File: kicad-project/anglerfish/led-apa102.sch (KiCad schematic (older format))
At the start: 2 parts

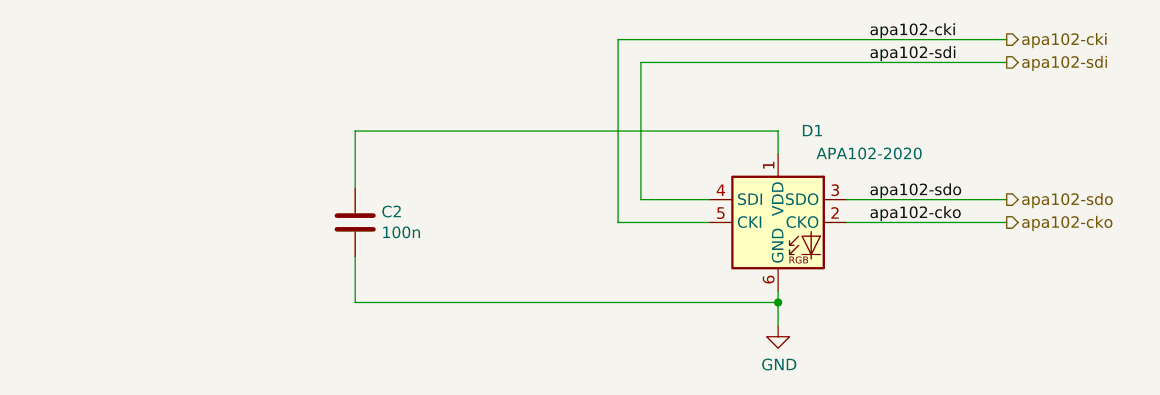
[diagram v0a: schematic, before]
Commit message: Generated gerbers. I discovered that I was working in a temp folder, so I erased the files under the anglerfish folder and manually brought the files from the temp folder.
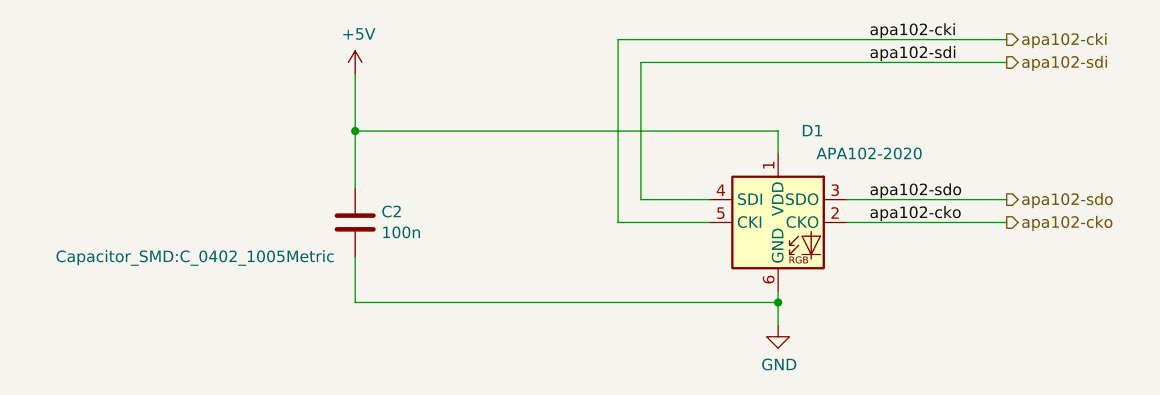
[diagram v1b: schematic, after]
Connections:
- net +5V: now reaches C2.1, D1.1 (VDD)
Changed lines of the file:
@@
 F 0 "C2" H 3615 3596 50  0000 L CNN
 F 1 "100n" H 3615 3505 50  0000 L CNN
-F 2 "Capacitor_SMD:C_0402_1005Metric" H 3538 3400 50  0001 C CNN
+F 2 "Capacitor_SMD:C_0402_1005Metric" H 2800 3400 50  0000 C CNN
 F 3 "~" H 3500 3550 50  0001 C CNN
 	1    3500 3550
@@
 Text Label 5750 2850 0    50   ~ 0
 apa102-sdi
+$Comp
+L power:+5V #PWR?
+U 1 1 604FC943
+P 3500 2900
+AR Path="/604FC943" Ref="#PWR?"  Part="1"
+AR Path="/60363A5D/604FC943" Ref="#PWR016"  Part="1"
+F 0 "#PWR016" H 3500 2750 50  0001 C CNN
+F 1 "+5V" H 3515 3073 50  0000 C CNN
+F 2 "" H 3500 2900 50  0001 C CNN
+F 3 "" H 3500 2900 50  0001 C CNN
+	1    3500 2900
+	1    0    0    -1
+$EndComp
+Wire Wire Line
+	3500 2900 3500 3150
+Connection ~ 3500 3150
 $EndSCHEMATC
